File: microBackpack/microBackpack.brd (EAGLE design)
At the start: 86.4 x 76.2 mm, 96 parts, among them IC1 LM324D, IC2 LM324D, J2 USB_B_PTH, J4 2X6 FEMALE, U1 ATMEGA328P_TQFP, U10 TLP185, U11 TLP185, U2 5VREG-HS, U3 CP2102N-QFN24, U4 TVS_DIODE_4PK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

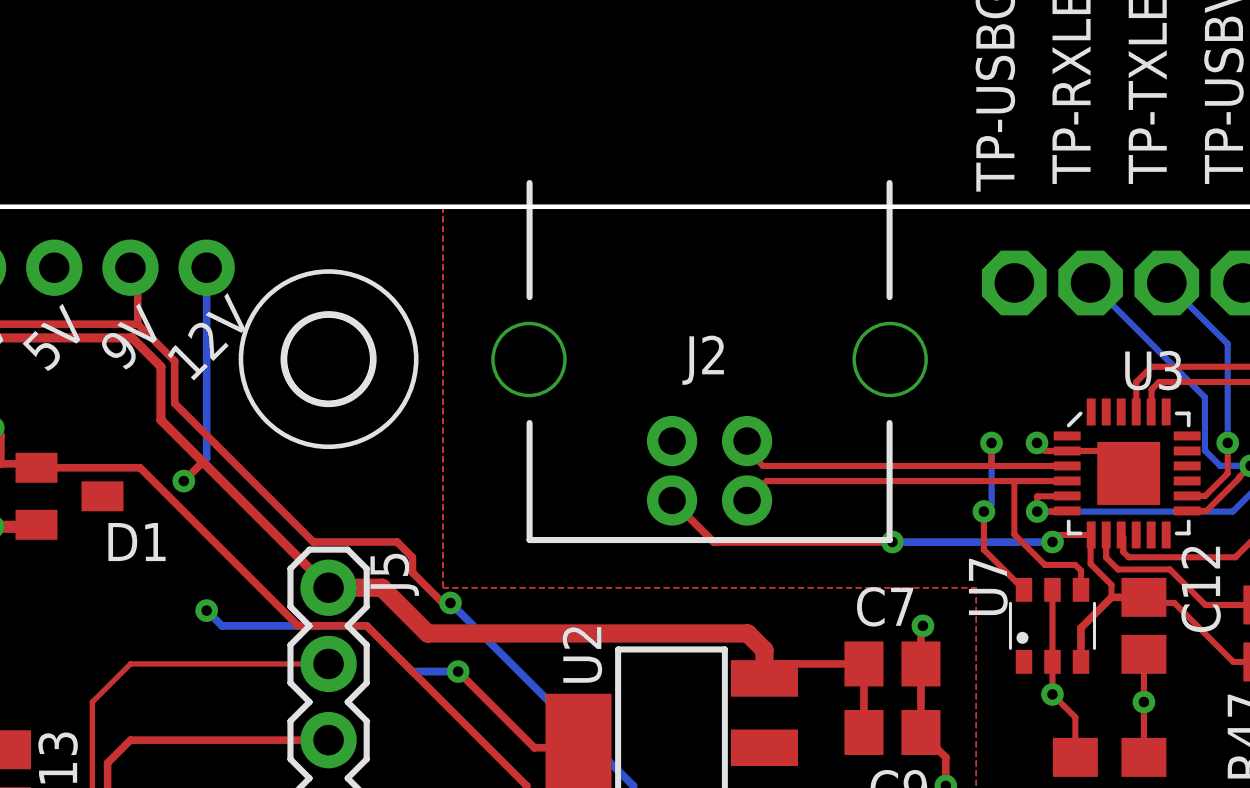
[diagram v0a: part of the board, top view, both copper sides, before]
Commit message: Added vertical USB. Ready to purchase
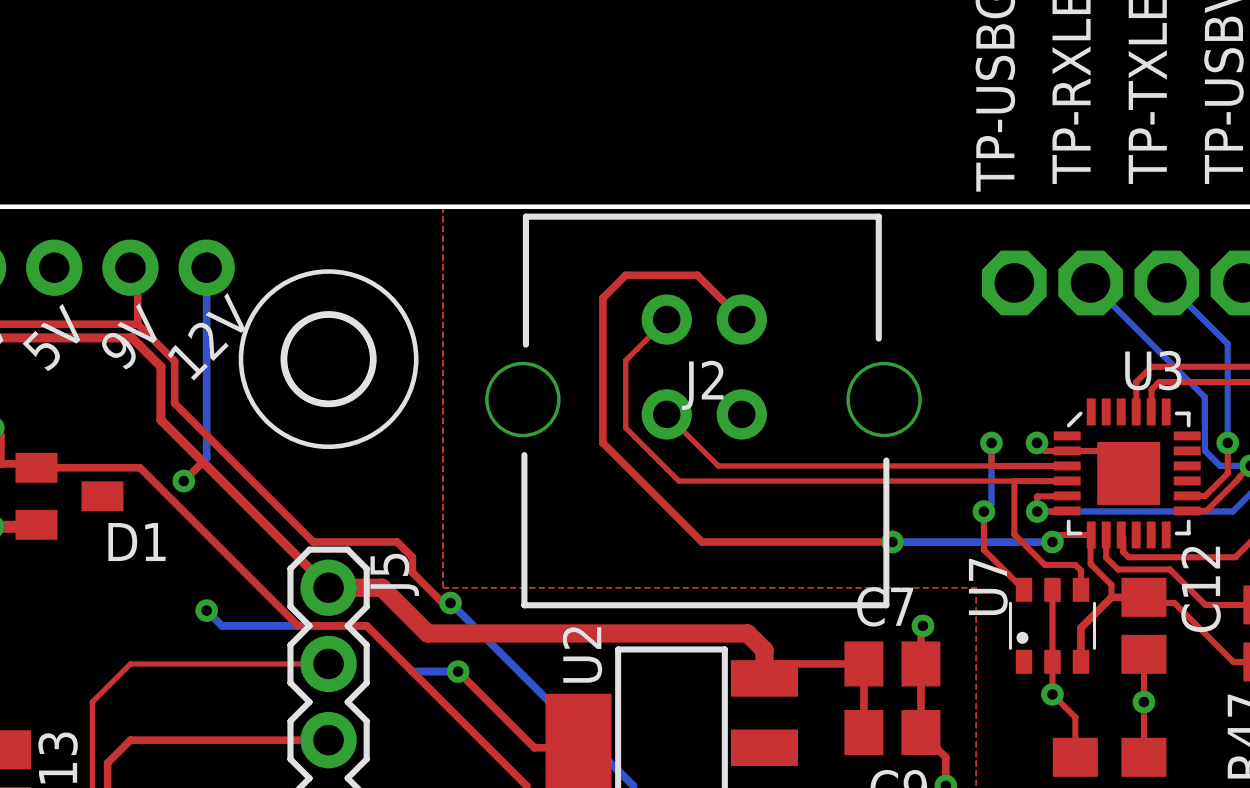
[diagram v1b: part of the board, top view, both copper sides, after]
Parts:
- J2: value USB_B_PTH -> USB_B; device SparkFun-Connectors:USB-B-PTH -> microBackpackLib:USB-B-PTH-VERT
- moved J2 3.13 mm to (43.0, 69.3), turned to 90 degrees
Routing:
- net VBUS: track 25.6 -> 39.1 mm
- net D-: track 16.1 -> 24.8 mm
- net D+: track 17.5 -> 20.4 mm
- net 12V: track 112.1 -> 111.3 mm
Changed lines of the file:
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@@
 <?xml version="1.0" encoding="utf-8"?>
 <!DOCTYPE eagle SYSTEM "eagle.dtd">
-<eagle version="9.4.2">
+<eagle version="9.1.2">
 <drawing>
 <settings>
@@
 <setting verticaltext="up"/>
 </settings>
-<grid distance="50" unitdist="mil" unit="mil" style="lines" multiple="4" display="no" altdistance="1" altunitdist="mil" altunit="mil"/>
+<grid distance="10" unitdist="mil" unit="mil" style="lines" multiple="4" display="no" altdistance="1" altunitdist="mil" altunit="mil"/>
 <layers>
 <layer number="1" name="Top" color="4" fill="1" visible="yes" active="yes"/>
@@
 </class>
 </classes>
-<designrules name="SilverCircuits">
+<designrules name="PCBway">
 <description language="en">&lt;b&gt;EAGLE Design Rules&lt;/b&gt;
 &lt;p&gt;
@@
 <attribute name="VALUE" x="57.658" y="30.607" size="1.016" layer="27" font="vector" rot="R270"/>
 </element>
-<element name="J2" library="SparkFun-Connectors" library_urn="urn:adsk.eagle:library:513" package="USB-B-PTH" package3d_urn="urn:adsk.eagle:package:38301/1" value="USB_B_PTH" x="43.18" y="72.39" smashed="yes" rot="R270">
-<attribute name="NAME" x="42.354" y="70.612" size="1.27" layer="25" font="vector" ratio="12"/>
-<attribute name="PROD_ID" value="CONN-08278" x="43.18" y="72.39" size="1.778" layer="27" rot="R270" display="off"/>
-<attribute name="SF_ID" value="PRT-00139" x="43.18" y="72.39" size="1.778" layer="27" rot="R270" display="off"/>
-<attribute name="VALUE" x="36.83" y="79.82" size="1.016" layer="27" font="vector" ratio="20" rot="R270" align="top-left"/>
+<element name="J2" library="microBackpackLib" package="USB-B-PTH-VERT" value="USB_B" x="42.9768" y="69.2658" smashed="yes" rot="R90">
+<attribute name="NAME" x="43.8028" y="71.0438" size="1.27" layer="25" font="vector" ratio="12" rot="R180"/>
+<attribute name="VALUE" x="42.7858" y="75.1332" size="1.016" layer="27" font="vector" ratio="20" align="top-left"/>
 </element>
 <element name="J3" library="SparkFun-Connectors" library_urn="urn:adsk.eagle:library:513" package="2X4" package3d_urn="urn:adsk.eagle:package:38103/1" value="" x="82.55" y="39.37" smashed="yes" rot="R270">
@@
 <wire x1="11.42640625" y1="69.9438" x2="7.2318" y2="69.9438" width="0.3048" layer="1"/>
 <contactref element="J6" pad="5"/>
-<wire x1="26.416" y1="74.168" x2="26.416" y2="73.406" width="0.254" layer="16"/>
-<wire x1="26.416" y1="67.818" x2="25.654" y2="67.056" width="0.254" layer="16"/>
+<wire x1="25.654" y1="67.056" x2="26.416" y2="67.818" width="0.254" layer="16"/>
 <via x="25.654" y="67.056" extent="1-16" drill="0.35"/>
 <wire x1="25.654" y1="67.056" x2="26.289" y2="67.691" width="0.254" layer="1"/>
-<wire x1="26.416" y1="74.168" x2="26.416" y2="67.818" width="0.254" layer="16"/>
+<wire x1="26.416" y1="67.818" x2="26.416" y2="74.168" width="0.254" layer="16"/>
 </signal>
 <signal name="4V_REF">
@@
 <wire x1="55.096" y1="67.056" x2="55.1" y2="67.06" width="0.254" layer="1"/>
 <contactref element="U7" pad="4"/>
-<wire x1="44.43" y1="66.4088" x2="45.0772" y2="67.056" width="0.2032" layer="1"/>
-<wire x1="45.0772" y1="67.056" x2="53.34" y2="67.056" width="0.2032" layer="1"/>
 <wire x1="53.34" y1="67.056" x2="55.096" y2="67.056" width="0.2032" layer="1"/>
 <wire x1="55.56" y1="63.43" x2="55.56" y2="64.074" width="0.2032" layer="1"/>
@@
 <wire x1="54.356" y1="64.262" x2="53.34" y2="65.278" width="0.2032" layer="1"/>
 <wire x1="53.34" y1="65.278" x2="53.34" y2="67.056" width="0.2032" layer="1"/>
+<wire x1="41.7522" y1="72.4408" x2="40.386" y2="71.0746" width="0.1778" layer="1"/>
+<wire x1="40.386" y1="68.82763125" x2="42.15763125" y2="67.056" width="0.1778" layer="1"/>
+<wire x1="40.386" y1="71.0746" x2="40.386" y2="68.82763125" width="0.1778" layer="1"/>
+<wire x1="42.15763125" y1="67.056" x2="53.34" y2="67.056" width="0.1778" layer="1"/>
 </signal>
 <signal name="D+">
@@
 <contactref element="J2" pad="D+"/>
 <contactref element="U7" pad="6"/>
-<wire x1="55.1" y1="67.56" x2="52.832" y2="67.56" width="0.2032" layer="1"/>
-<wire x1="44.962" y1="67.56" x2="52.578" y2="67.56" width="0.2032" layer="1"/>
-<wire x1="52.578" y1="67.56" x2="52.832" y2="67.56" width="0.2032" layer="1"/>
-<wire x1="44.43" y1="68.092" x2="44.43" y2="68.39" width="0.2032" layer="1"/>
-<wire x1="44.962" y1="67.56" x2="44.43" y2="68.092" width="0.2032" layer="1"/>
+<wire x1="55.1" y1="67.56" x2="52.578" y2="67.56" width="0.2032" layer="1"/>
 <wire x1="52.578" y1="67.56" x2="52.578" y2="68.326" width="0.2032" layer="1"/>
 <via x="52.578" y="68.326" extent="1-16" drill="0.35"/>
@@
 <wire x1="52.324" y1="66.04" x2="52.324" y2="64.766" width="0.2032" layer="1"/>
 <wire x1="52.324" y1="64.766" x2="53.66" y2="63.43" width="0.2032" layer="1"/>
+<wire x1="41.7522" y1="69.278" x2="43.4702" y2="67.56" width="0.1778" layer="1"/>
+<wire x1="43.4702" y1="67.56" x2="52.578" y2="67.56" width="0.1778" layer="1"/>
 </signal>
 <signal name="VBUS">
@@
 <contactref element="R47" pad="2"/>
 <contactref element="C12" pad="1"/>
-<wire x1="41.93" y1="66.4088" x2="43.3148" y2="65.024" width="0.254" layer="1"/>
 <contactref element="U7" pad="3"/>
 <wire x1="55.56" y1="61.03" x2="55.56" y2="62.164" width="0.254" layer="1"/>
 <wire x1="56.576" y1="63.18" x2="57.658" y2="63.18" width="0.254" layer="1"/>
 <wire x1="55.56" y1="62.164" x2="56.576" y2="63.18" width="0.254" layer="1"/>
-<wire x1="43.3148" y1="65.024" x2="49.276" y2="65.024" width="0.254" layer="1"/>
 <via x="49.276" y="65.024" extent="1-16" drill="0.35"/>
 <wire x1="49.276" y1="65.024" x2="54.61" y2="65.024" width="0.254" layer="16"/>
@@
 <wire x1="60.64" y1="61.026" x2="61.722" y2="61.026" width="0.2032" layer="1"/>
 <wire x1="58.674" y1="62.992" x2="60.64" y2="61.026" width="0.2032" layer="1"/>
+<wire x1="44.2522" y1="72.4408" x2="42.779" y2="73.914" width="0.254" layer="1"/>
+<wire x1="42.926" y1="65.024" x2="49.276" y2="65.024" width="0.254" layer="1"/>
+<wire x1="42.779" y1="73.914" x2="40.386" y2="73.914" width="0.254" layer="1"/>
+<wire x1="40.386" y1="73.914" x2="39.624" y2="73.152" width="0.254" layer="1"/>
+<wire x1="39.624" y1="73.152" x2="39.624" y2="68.326" width="0.254" layer="1"/>
+<wire x1="39.624" y1="68.326" x2="42.926" y2="65.024" width="0.254" layer="1"/>
 </signal>
 <signal name="N$7">

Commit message: rerouted fgen and crystal as diff pair. Should be better for high frequency
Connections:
- net N$1 renamed CRYS_P
- net N$2 renamed CRYS_N
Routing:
- net FGEN: track 70.1 -> 88.9 mm, vias 6 -> 5
- net CRYS_N: track 14.2 -> 20.9 mm
- net CRYS_P: track 19.1 -> 21.5 mm
- net LDAC: track 40.1 -> 42.2 mm
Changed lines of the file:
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@@
 <?xml version="1.0" encoding="utf-8"?>
 <!DOCTYPE eagle SYSTEM "eagle.dtd">
-<eagle version="9.1.2">
+<eagle version="9.4.2">
 <drawing>
 <settings>
@@
 <class number="0" name="default" width="0" drill="0">
 </class>
+<class number="1" name="crystalDiff" width="0.254" drill="0">
+</class>
 </classes>
-<designrules name="PCBway">
+<designrules name="SilverCircuits">
 <description language="en">&lt;b&gt;EAGLE Design Rules&lt;/b&gt;
 &lt;p&gt;
@@
 </elements>
 <signals>
-<signal name="N$1">
+<signal name="CRYS_P" class="1">
 <contactref element="Q1" pad="2"/>
 <contactref element="U1" pad="8"/>
@@
 <wire x1="27.874" y1="13.97" x2="30.607" y2="13.97" width="0.254" layer="1"/>
 <wire x1="30.607" y1="13.97" x2="32.004" y2="12.573" width="0.254" layer="1"/>
-<wire x1="32.004" y1="12.573" x2="32.004" y2="12.7" width="0.254" layer="1"/>
-<wire x1="33.02" y1="17.78" x2="32.512" y2="18.288" width="0.254" layer="1"/>
-<wire x1="32.512" y1="18.288" x2="32.512" y2="24.9962" width="0.254" layer="1"/>
-<wire x1="32.512" y1="24.9962" x2="33.488571875" y2="25.972771875" width="0.254" layer="1"/>
-<wire x1="32.004" y1="12.7" x2="33.02" y2="13.716" width="0.254" layer="1"/>
-<wire x1="33.02" y1="13.716" x2="33.02" y2="17.78" width="0.254" layer="1"/>
+<wire x1="32.004" y1="13.5636" x2="33.274" y2="14.8336" width="0.254" layer="1"/>
+<wire x1="33.274" y1="14.8336" x2="33.4528625" y2="14.8336" width="0.254" layer="1"/>
+<wire x1="33.4528625" y1="14.8336" x2="34.2138" y2="15.5945375" width="0.254" layer="1"/>
+<wire x1="34.2138" y1="19.9908625" x2="31.29333125" y2="22.91133125" width="0.254" layer="1"/>
+<wire x1="31.29333125" y1="22.91133125" x2="31.29333125" y2="24.18133125" width="0.254" layer="1"/>
+<wire x1="31.29333125" y1="24.18133125" x2="32.004" y2="24.892" width="0.254" layer="1"/>
+<wire x1="32.407796875" y1="24.892" x2="33.488571875" y2="25.972775" width="0.254" layer="1"/>
+<wire x1="33.488571875" y1="25.972775" x2="33.488571875" y2="25.972771875" width="0.254" layer="1"/>
+<wire x1="32.004" y1="24.892" x2="32.407796875" y2="24.892" width="0.254" layer="1"/>
+<wire x1="34.2138" y1="15.5945375" x2="34.2138" y2="19.9908625" width="0.254" layer="1"/>
+<wire x1="32.004" y1="12.573" x2="32.004" y2="13.5636" width="0.254" layer="1"/>
 </signal>
-<signal name="N$2">
+<signal name="CRYS_N" class="1">
 <contactref element="Q1" pad="1"/>
 <contactref element="C2" pad="1"/>
@@
 <wire x1="27.874" y1="16.002" x2="30.607" y2="16.002" width="0.254" layer="1"/>
 <wire x1="30.607" y1="16.002" x2="32.004" y2="17.399" width="0.254" layer="1"/>
-<wire x1="32.922884375" y1="26.538459375" x2="32.004" y2="25.619575" width="0.254" layer="1"/>
-<wire x1="32.004" y1="25.619575" x2="32.004" y2="17.399" width="0.254" layer="1"/>
+<wire x1="32.004" y1="17.399" x2="32.004" y2="16.5354" width="0.254" layer="1"/>
+<wire x1="32.004" y1="16.5354" x2="33.274" y2="15.2654" width="0.254" layer="1"/>
+<wire x1="33.274" y1="15.2654" x2="33.782" y2="15.7734" width="0.254" layer="1"/>
+<wire x1="30.86153125" y1="22.73246875" x2="30.86153125" y2="24.36019375" width="0.254" layer="1"/>
+<wire x1="30.86153125" y1="24.36019375" x2="31.69866875" y2="25.19733125" width="0.254" layer="1"/>
+<wire x1="31.69866875" y1="25.314240625" x2="32.9228875" y2="26.538459375" width="0.254" layer="1"/>
+<wire x1="32.9228875" y1="26.538459375" x2="32.922884375" y2="26.538459375" width="0.254" layer="1"/>
+<wire x1="31.69866875" y1="25.19733125" x2="31.69866875" y2="25.314240625" width="0.254" layer="1"/>
+<wire x1="33.782" y1="15.7734" x2="33.782" y2="19.812" width="0.254" layer="1"/>
+<wire x1="33.782" y1="19.812" x2="30.86153125" y2="22.73246875" width="0.254" layer="1"/>
 </signal>
 <signal name="GND">
@@
 <contactref element="U5" pad="4"/>
 <contactref element="U1" pad="14"/>
-<wire x1="38.427853125" y1="28.8012" x2="39.0398" y2="28.189253125" width="0.254" layer="1"/>
-<wire x1="39.0398" y1="21.1582" x2="39.34441875" y2="20.85358125" width="0.254" layer="1"/>
-<via x="39.34441875" y="20.85358125" extent="1-16" drill="0.35"/>
-<wire x1="39.0398" y1="28.189253125" x2="39.0398" y2="21.1582" width="0.254" layer="1"/>
 <wire x1="13.2" y1="33.51" x2="13.208" y2="33.502" width="0.2032" layer="1"/>
 <wire x1="13.208" y1="33.502" x2="13.208" y2="32.766" width="0.2032" layer="1"/>
 <wire x1="13.208" y1="32.766" x2="16.256" y2="29.718" width="0.2032" layer="1"/>
 <via x="22.098" y="29.718" extent="1-16" drill="0.254"/>
-<wire x1="25.654" y1="29.718" x2="22.098" y2="29.718" width="0.2032" layer="16"/>
 <wire x1="16.256" y1="29.718" x2="22.098" y2="29.718" width="0.2032" layer="1"/>
-<wire x1="39.34441875" y1="20.85358125" x2="34.51841875" y2="20.85358125" width="0.2032" layer="16"/>
-<wire x1="34.51841875" y1="20.85358125" x2="25.654" y2="29.718" width="0.2032" layer="16"/>
+<wire x1="22.098" y1="29.718" x2="23.876" y2="27.94" width="0.254" layer="16"/>
+<wire x1="23.876" y1="27.94" x2="23.876" y2="26.924" width="0.254" layer="16"/>
+<wire x1="23.876" y1="26.924" x2="25.146" y2="25.654" width="0.254" layer="16"/>
+<wire x1="27.432" y1="25.654" x2="29.464" y2="23.622" width="0.254" layer="16"/>
+<wire x1="29.464" y1="23.622" x2="32.766" y2="23.622" width="0.254" layer="16"/>
+<wire x1="32.766" y1="23.622" x2="34.798" y2="21.59" width="0.254" layer="16"/>
+<wire x1="40.386" y1="21.59" x2="40.64" y2="21.336" width="0.254" layer="16"/>
+<via x="40.64" y="21.336" extent="1-16" drill="0.35"/>
+<wire x1="25.146" y1="25.654" x2="27.432" y2="25.654" width="0.254" layer="16"/>
+<wire x1="34.798" y1="21.59" x2="40.386" y2="21.59" width="0.254" layer="16"/>
+<wire x1="39.116" y1="28.113053125" x2="39.116" y2="22.352" width="0.254" layer="1"/>
+<wire x1="39.116" y1="22.352" x2="40.132" y2="21.336" width="0.254" layer="1"/>
+<wire x1="40.132" y1="21.336" x2="40.64" y2="21.336" width="0.254" layer="1"/>
+<wire x1="38.427853125" y1="28.8012" x2="39.116" y2="28.113053125" width="0.254" layer="1"/>
 </signal>
 <signal name="DAC_A">
@@
 <wire x1="13.2" y1="37.61" x2="13.2" y2="38.346" width="0.2032" layer="1"/>
 <wire x1="13.2" y1="38.346" x2="13.462" y2="38.608" width="0.2032" layer="1"/>
-<wire x1="13.462" y1="38.608" x2="13.74713125" y2="38.608" width="0.2032" layer="1"/>
-<wire x1="14.224" y1="38.13113125" x2="13.74713125" y2="38.608" width="0.2032" layer="1"/>
+<wire x1="13.462" y1="38.608" x2="14.00113125" y2="38.608" width="0.2032" layer="1"/>
+<wire x1="14.224" y1="38.38513125" x2="14.00113125" y2="38.608" width="0.2032" layer="1"/>
 <wire x1="18.94626875" y1="30.3786" x2="18.84486875" y2="30.48" width="0.2032" layer="1"/>
 <wire x1="18.84486875" y1="30.48" x2="18.796" y2="30.48" width="0.2032" layer="1"/>
@@
 <wire x1="21.1686" y1="30.3786" x2="18.94626875" y2="30.3786" width="0.2032" layer="1"/>
 <wire x1="18.796" y1="30.48" x2="14.224" y2="35.052" width="0.2032" layer="1"/>
-<wire x1="14.224" y1="35.052" x2="14.224" y2="38.13113125" width="0.2032" layer="1"/>
+<wire x1="14.224" y1="35.052" x2="14.224" y2="38.38513125" width="0.2032" layer="1"/>
 </signal>
 <signal name="DAC_C">
@@
 <wire x1="26.416" y1="33.782" x2="26.416" y2="30.226" width="0.254" layer="16"/>
 <via x="26.416" y="30.226" extent="1-16" drill="0.35"/>
-<wire x1="26.416" y1="30.226" x2="26.416" y2="27.432" width="0.254" layer="1"/>
-<via x="26.416" y="27.432" extent="1-16" drill="0.35"/>
-<wire x1="26.416" y1="27.432" x2="35.306" y2="18.542" width="0.254" layer="16"/>
-<wire x1="35.306" y1="18.542" x2="37.084" y2="18.542" width="0.254" layer="16"/>
-<via x="37.084" y="18.542" extent="1-16" drill="0.35"/>
-<wire x1="37.084" y1="18.542" x2="46.99" y2="8.636" width="0.254" layer="1"/>
-<wire x1="46.99" y1="8.636" x2="46.99" y2="6.35" width="0.254" layer="1"/>
+<wire x1="46.99" y1="6.35" x2="46.99" y2="9.398" width="0.254" layer="16"/>
+<wire x1="46.99" y1="9.398" x2="46.482" y2="9.906" width="0.254" layer="16"/>
+<via x="22.86" y="23.622" extent="1-16" drill="0.35"/>
+<wire x1="26.416" y1="23.622" x2="22.86" y2="23.622" width="0.254" layer="1"/>
+<wire x1="46.482" y1="9.906" x2="39.878" y2="9.906" width="0.254" layer="16"/>
+<wire x1="39.878" y1="9.906" x2="37.084" y2="7.112" width="0.254" layer="16"/>
+<wire x1="37.084" y1="7.112" x2="35.052" y2="7.112" width="0.254" layer="16"/>
+<wire x1="35.052" y1="7.112" x2="33.274" y2="8.89" width="0.254" layer="16"/>
+<wire x1="33.274" y1="8.89" x2="26.162" y2="8.89" width="0.254" layer="16"/>
+<wire x1="26.162" y1="8.89" x2="22.86" y2="12.192" width="0.254" layer="16"/>
+<wire x1="22.86" y1="12.192" x2="22.86" y2="23.622" width="0.254" layer="16"/>
+<wire x1="26.416" y1="30.226" x2="26.416" y2="23.622" width="0.254" layer="1"/>
 </signal>
 <signal name="N$11">
